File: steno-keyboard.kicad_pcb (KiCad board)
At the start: 2 copper layers, 26 parts, among them SW1 SW_Push, SW10 SW_Push, SW11 SW_Push, SW12 SW_Push, SW13 SW_Push, SW14 SW_Push, SW15 SW_Push, SW16 SW_Push, SW17 SW_Push, SW18 SW_Push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

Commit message: Organized PCB
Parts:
- moved A1 146.3 mm to (191.1, 109.7)
- moved SW1 81.9 mm to (85.7, 104.8)
- moved SW5 81.9 mm to (161.9, 104.8)
- moved SW6 81.9 mm to (219.1, 104.8)
- moved SW10 74.4 mm to (295.3, 95.2)
- moved SW11 74.4 mm to (314.3, 95.2)
- moved SW12 74.4 mm to (104.8, 114.3)
- moved SW13 74.4 mm to (123.8, 114.3)
- moved SW14 74.4 mm to (142.9, 114.3)
- moved SW15 74.4 mm to (238.1, 114.3)
- moved SW16 74.4 mm to (257.2, 114.3)
- moved SW17 74.4 mm to (276.2, 114.3)
- moved SW18 74.4 mm to (295.3, 114.3)
- moved SW19 74.4 mm to (314.3, 114.3)
- moved SW2 74.4 mm to (104.8, 95.2)
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
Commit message: Added traces for PWR
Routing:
- net /PWR: track 0.00 -> 650.0 mm
- net /BTN0: track 0.00 -> 99.0 mm
- net /BTN1: track 0.00 -> 75.0 mm
- net /BTN2: track 0.00 -> 57.6 mm
- net /BTN3: track 0.00 -> 38.3 mm
- net /BTN4: track 0.00 -> 17.6 mm

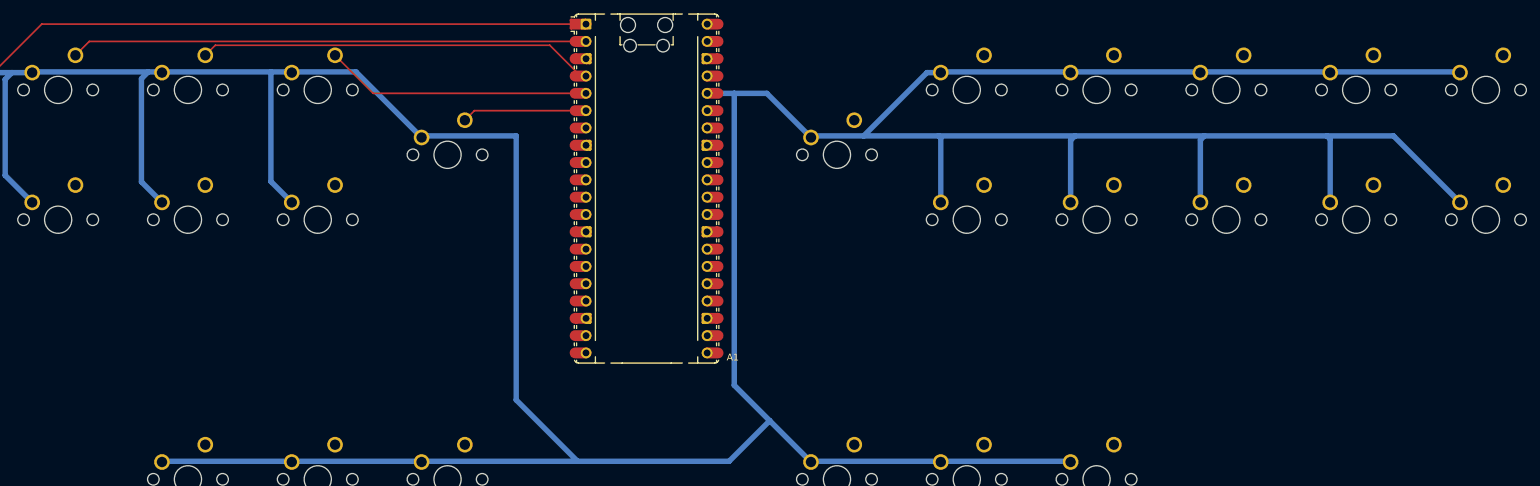
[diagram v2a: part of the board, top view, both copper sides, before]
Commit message: Finished PCB and rerouted some wires
Although the layout is messy, it allows for clean routing of the GPIOs
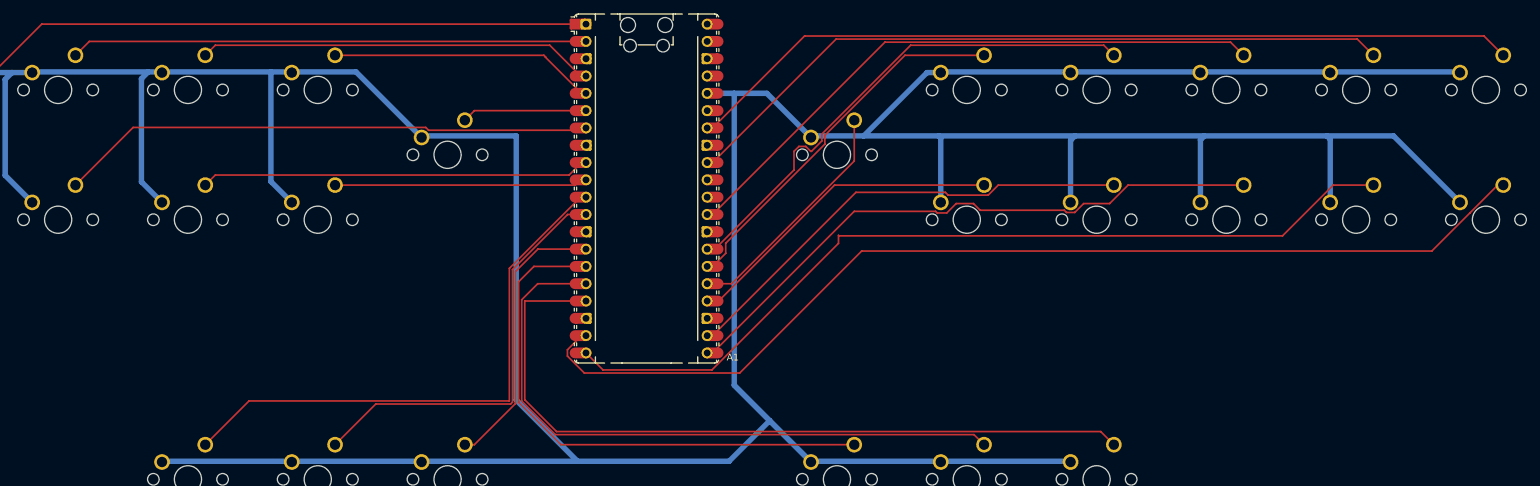
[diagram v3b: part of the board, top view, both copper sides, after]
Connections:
- A1 pad 10: /BTN7 -> /BTN13
- A1 pad 11: /BTN8 -> /BTN19
- A1 pad 12: /BTN9 -> /BTN20
- A1 pad 14: /BTN10 -> /BTN21
- A1 pad 15: /BTN11 -> /BTN22
- A1 pad 16: /BTN12 -> /BTN23
- A1 pad 17: /BTN13 -> /BTN24
- A1 pad 19: /BTN14 -> /BTN18
- A1 pad 20: /BTN15 -> /BTN17
- A1 pad 22: /BTN17 -> /BTN15
- A1 pad 24: /BTN18 -> /BTN14
- A1 pad 25: /BTN19 -> /BTN5
- A1 pad 26: /BTN20 -> /BTN6
- A1 pad 27: /BTN21 -> /BTN7
- A1 pad 29: /BTN22 -> /BTN8
- A1 pad 32: /BTN23 -> /BTN9
- A1 pad 34: /BTN24 -> /BTN10
- A1 pad 7: /BTN5 -> /BTN11
- A1 pad 9: /BTN6 -> /BTN12
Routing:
- net /BTN18: track 0.00 -> 154.3 mm
- net /BTN17: track 0.00 -> 128.6 mm
- net /BTN10: track 0.00 -> 122.8 mm
- net /BTN24: track 0.00 -> 111.9 mm
- net /BTN9: track 0.00 -> 105.5 mm
- net /BTN23: track 0.00 -> 95.8 mm
- net /BTN16: track 0.00 -> 89.4 mm
- net /BTN8: track 0.00 -> 89.2 mm
- net /BTN19: track 0.00 -> 81.5 mm
- net /BTN22: track 0.00 -> 80.4 mm
- net /BTN11: track 0.00 -> 78.7 mm
- net /BTN7: track 0.00 -> 75.5 mm
- net /BTN15: track 0.00 -> 68.4 mm
- net /BTN20: track 0.00 -> 62.2 mm
- net /BTN12: track 0.00 -> 57.2 mm
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
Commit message: Small fix to connection BTN17
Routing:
- net /BTN17: track 128.6 -> 131.3 mm
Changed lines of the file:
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@@
 	)
 	(segment
-		(start 219.3 117.772406)
-		(end 219.3 116.6)
-		(width 0.25)
-		(layer "F.Cu")
-		(net 16)
-	)
-	(segment
-		(start 219.3699 116.6699)
-		(end 284.46772 116.6699)
-		(width 0.25)
-		(layer "F.Cu")
-		(net 16)
-	)
-	(segment
-		(start 200.721481 136.350925)
-		(end 219.3 117.772406)
-		(width 0.25)
-		(layer "F.Cu")
-		(net 16)
-	)
-	(segment
-		(start 291.91762 109.22)
-		(end 297.815 109.22)
+		(start 294.526545 118.4)
+		(end 297.815 115.111545)
 		(width 0.25)
 		(layer "F.Cu")
@@
 	)
 	(segment
-		(start 219.3 116.6)
-		(end 219.3699 116.6699)
-		(width 0.25)
-		(layer "F.Cu")
-		(net 16)
-	)
-	(segment
-		(start 284.46772 116.6699)
-		(end 291.91762 109.22)
+		(start 221.650925 118.4)
+		(end 294.526545 118.4)
 		(width 0.25)
 		(layer "F.Cu")
@@
 	(segment
 		(start 184.740925 136.350925)
-		(end 200.721481 136.350925)
+		(end 203.7 136.350925)
 		(width 0.25)
 		(layer "F.Cu")
+		(net 16)
+	)
+	(segment
+		(start 297.815 115.111545)
+		(end 297.815 109.22)
+		(width 0.25)
+		(layer "F.Cu")
+		(net 16)
+	)
+	(segment
+		(start 203.7 136.350925)
+		(end 221.650925 118.4)
+		(width 0.25)
+		(layer "F.Cu")

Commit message: Finished PCB
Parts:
- added H1: MountingHole_3.2mm_M3, MountingHole:MountingHole_3.2mm_M3, F.Cu at (85.0, 123.0)
- added H1: MountingHole_3.2mm_M3, MountingHole:MountingHole_3.2mm_M3, F.Cu at (85.0, 89.0)
- added H2: MountingHole_3.2mm_M3, MountingHole:MountingHole_3.2mm_M3, F.Cu at (257.2, 133.3)
- added H3: MountingHole_3.2mm_M3, MountingHole:MountingHole_3.2mm_M3, F.Cu at (192.0, 153.0)
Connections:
- A1 pad 33: unconnected-(A1-AGND-Pad33) -> GND
- A1 pad 36: /PWR -> unconnected-(A1-3V3-Pad36)
- SW1 pad 1: /PWR -> GND
- SW10 pad 1: /PWR -> GND
- SW11 pad 1: /PWR -> GND
- SW12 pad 1: /PWR -> GND
- SW13 pad 1: /PWR -> GND
- SW14 pad 1: /PWR -> GND
- SW15 pad 1: /PWR -> GND
- SW16 pad 1: /PWR -> GND
- SW17 pad 1: /PWR -> GND
- SW18 pad 1: /PWR -> GND
- SW19 pad 1: /PWR -> GND
- SW2 pad 1: /PWR -> GND
- SW20 pad 1: /PWR -> GND
- SW21 pad 1: /PWR -> GND
- SW22 pad 1: /PWR -> GND
- SW23 pad 1: /PWR -> GND
- SW24 pad 1: /PWR -> GND
- SW25 pad 1: /PWR -> GND
- SW3 pad 1: /PWR -> GND
- SW4 pad 1: /PWR -> GND
- SW5 pad 1: /PWR -> GND
- SW6 pad 1: /PWR -> GND
- SW7 pad 1: /PWR -> GND
- SW8 pad 1: /PWR -> GND
- SW9 pad 1: /PWR -> GND
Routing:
- net /PWR: track 650.0 -> 0.00 mm
- net /BTN18: track 154.3 -> 172.7 mm
- net /BTN17: track 131.3 -> 144.7 mm
- net /BTN19: track 81.5 -> 70.9 mm
- net /BTN22: track 80.4 -> 87.6 mm
- net /BTN5: track 34.2 -> 40.9 mm
- net /BTN6: track 54.3 -> 60.9 mm
- net /BTN8: track 89.2 -> 95.0 mm
- net /BTN7: track 75.5 -> 80.5 mm
- net /BTN20: track 62.2 -> 58.6 mm
- net /BTN15: track 68.4 -> 71.8 mm
- net /BTN9: track 105.5 -> 108.8 mm
- net /BTN23: track 95.8 -> 98.8 mm
- net /BTN24: track 111.9 -> 109.6 mm
- net /BTN10: track 122.8 -> 124.9 mm
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- added copper zone on B.Cu, net GND
- added copper zone on F.Cu, net GND
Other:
- board outline added: 254 x 82 mm
- board text added: "Steno Mk. 1 by Owen"

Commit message: Updated PCB's labels
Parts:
- renumbered H1 to H2, H2 to H4
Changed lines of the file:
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@@
 		(descr "Mounting Hole 3.2mm, M3, no annular, generated by kicad-footprint-generator mountinghole.py")
 		(tags "mountinghole M3")
-		(property "Reference" "H1"
+		(property "Reference" "H2"
 			(at 0 -4.15 0)
 			(layer "F.SilkS")
@@
 		(descr "Mounting Hole 3.2mm, M3, no annular, generated by kicad-footprint-generator mountinghole.py")
 		(tags "mountinghole M3")
-		(property "Reference" "H2"
+		(property "Reference" "H4"
 			(at 0 -4.15 0)
 			(layer "F.SilkS")
